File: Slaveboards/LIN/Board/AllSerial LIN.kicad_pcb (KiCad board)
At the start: 2 copper layers, 67.4 x 44.8 mm, 13 parts, among them IC6 MCP2003, J1 MA02-1W, X1 ALLSERIALSLAVE, X6 AKL18X-03W

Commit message: Improve libraries
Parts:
- moved X6 1.27 mm to (161.2, 91.2)
- moved D2 1.15 mm to (157.9, 100.1)
- moved C1 0.82 mm to (159.3, 95.2)
- moved J1 0.49 mm to (134.5, 91.7)
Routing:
- net Net-(D2-K): track 42.5 -> 43.9 mm
- net GND: track 10.8 -> 11.6 mm, vias 43 -> 42
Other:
- board text added: "AllSerial - LIN v1.3 27/25"
- board text removed: "AllSerial - LIN v1.2 25/23"
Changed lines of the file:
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@@
 	(footprint "Diode_SMD:D_SMB"
 		(layer "F.Cu")
-		(at 157.8991 98.9556 180)
+		(at 157.8991 100.1036 180)
 		(descr "Diode SMB (DO-214AA)")
 		(tags "Diode SMB (DO-214AA)")
@@
 	(footprint "Connector_PinHeader_2.54mm:PinHeader_1x02_P2.54mm_Horizontal"
 		(layer "F.Cu")
-		(at 134.5311 91.2086 90)
+		(at 134.5311 91.7036 90)
 		(descr "Through hole angled pin header, 1x02, 2.54mm pitch, 6mm pin length, single row")
 		(tags "Through hole angled pin header THT 1x02 2.54mm single row")
@@
 	(footprint "AllSerial:Metz_PT11303HBBN_182"
 		(layer "F.Cu")
-		(at 161.2011 89.9386 180)
+		(at 161.2011 91.2036 180)
 		(property "Reference" "X6"
 			(at -0.7989 -4.0614 180)
@@
 	(footprint "Capacitor_SMD:C_0805_2012Metric"
 		(layer "F.Cu")
-		(at 159.2961 94.3836 180)
+		(at 159.2961 95.2036 180)
 		(descr "Capacitor SMD 0805 (2012 Metric), square (rectangular) end terminal, IPC_7351 nominal, (Body size source: IPC-SM-782 page 76, https://www.pcb-3d.com/wordpress/wp-content/uploads/ipc-sm-782a_amendment_1_and_2.pdf, https://docs.google.com/spreadsheets/d/1BsfQQcO9C6DZCsRaXUlFlo91Tg2WpOkGARC1WS5S8t0/edit?usp=sharing), generated with kicad-footprint-generator")
 		(tags "capacitor")
@@
 			(stroke
 				(width 0.1)
-				(type solid)
+				(type dash)
+			)
+			(layer "Dwgs.User")
+		)
+		(fp_line
+			(start -35.75 -45.8)
+			(end 35.75 -45.8)
+			(stroke
+				(width 0.1)
+				(type dash)
 			)
 			(layer "Dwgs.User")
@@
 		)
 		(embedded_fonts no)
-		(model ":KICAD9_3DMODEL_DIR:Connector_PinHeader_2.54mm.3dshapes/PinHeader_2x10_P2.54mm_Horizontal.step"
+		(model "$(KICAD8_3DMODEL_DIR)/Connector_PinHeader_2.54mm.3dshapes/PinHeader_2x10_P2.54mm_Horizontal.step"
 			(offset
 				(xyz 11.43 7 0)
@@
 			)
 		)
-		(model "../Front/AllSerial LIN Front.step"
+		(model "${KICAD9_3RD_PARTY}/packages3d/Fischer AKG 71 24 100 bottom half.step"
+			(offset
+				(xyz 35.8 44.8 1.85)
+			)
+			(scale
+				(xyz 1 1 1)
+			)
+			(rotate
+				(xyz 90 0 -180)
+			)
+		)
+		(model "C:/Users/StefanSeegel/Dropbox/Projekte/AllSerial Repo/Slaveboards/LIN/Front/AllSerial LIN Front.step"
 			(offset
-				(xyz 0 44.8 -7.2)
+				(xyz 0 44.8 -7.25)
 			)
 			(scale
@@
 		)
 	)
-	(gr_text "AllSerial - LIN v1.2 25/23"
+	(gr_text "AllSerial - LIN v1.3 27/25"
 		(at 118.0211 118.5136 90)
 		(layer "F.SilkS")
@@
 	)
 	(segment
-		(start 158.3461 94.3836)
-		(end 158.3461 93.4336)
+		(start 158.3461 93.4336)
+		(end 157.7011 92.7886)
 		(width 0.4064)
 		(layer "F.Cu")
@@
 	)
 	(segment
-		(start 157.7011 92.7886)
+		(start 158.3461 95.2036)
 		(end 158.3461 93.4336)
 		(width 0.4064)
@@
 	)
 	(segment
-		(start 159.2961 105.5596)
-		(end 160.3121 105.5596)
+		(start 157.7011 92.7886)
+		(end 157.7011 89.9386)
 		(width 0.4064)
 		(layer "F.Cu")
@@
 	)
 	(segment
-		(start 153.5811 109.3036)
-		(end 153.5811 110.8936)
+		(start 159.2961 105.5596)
+		(end 160.3121 105.5596)
 		(width 0.4064)
 		(layer "F.Cu")
@@
 	)
 	(segment
-		(start 157.7011 89.9386)
-		(end 157.7011 92.7886)
+		(start 153.5811 109.3036)
+		(end 153.5811 110.8936)
 		(width 0.4064)
 		(layer "F.Cu")
@@
 	)
 	(via
-		(at 148.5011 114.7036)
-		(size 0.6048)
-		(drill 0.3)
-		(layers "F.Cu" "B.Cu")
-		(net 1)
-	)
-	(via
 		(at 173.9011 114.7036)
 		(size 0.6048)
@@
 	)
 	(segment
-		(start 137.0711 120.4186)
-		(end 137.0711 119.7836)
+		(start 147.2311 114.7036)
+		(end 142.1511 119.7836)
 		(width 0.4064)
 		(layer "F.Cu")
@@
 	)
 	(segment
-		(start 148.5011 115.9736)
-		(end 145.9611 115.9736)
+		(start 137.0711 120.4186)
+		(end 137.0711 119.7836)
 		(width 0.4064)
 		(layer "F.Cu")
@@
 	)
 	(segment
-		(start 145.9611 115.9736)
-		(end 142.1511 119.7836)
-		(width 0.4064)
-		(layer "F.Cu")
-		(net 2)
-	)
-	(segment
 		(start 156.7561 111.1476)
 		(end 156.7561 114.0686)
@@
 	)
 	(segment
-		(start 149.7711 114.7036)
-		(end 148.5011 115.9736)
+		(start 151.0411 114.7036)
+		(end 147.2311 114.7036)
 		(width 0.4064)
 		(layer "F.Cu")
@@
 	)
 	(segment
-		(start 151.0411 114.7036)
-		(end 149.7711 114.7036)
-		(width 0.4064)
-		(layer "F.Cu")
-		(net 2)
-	)
-	(segment
 		(start 140.8811 118.5136)
 		(end 142.1511 119.7836)
@@
 	)
 	(segment
-		(start 161.2011 89.9386)
+		(start 160.2461 96.1616)
+		(end 160.2461 97.3036)
+		(width 0.4)
+		(layer "F.Cu")
+		(net 18)
+	)
+	(segment
+		(start 160.2461 94.0686)
 		(end 161.2011 93.1136)
 		(width 0.4064)
@@
 	)
 	(segment
+		(start 160.2461 96.1616)
+		(end 160.2461 95.2036)
+		(width 0.4)
+		(layer "F.Cu")
+		(net 18)
+	)
+	(segment
 		(start 159.9311 101.4956)
 		(end 159.9311 99.0736)
@@
 	)
 	(segment
-		(start 151.9301 91.2086)
-		(end 137.0711 91.2086)
-		(width 0.4)
+		(start 161.2011 93.1136)
+		(end 161.2011 89.9386)
+		(width 0.4064)
 		(layer "F.Cu")
 		(net 18)
@@
 	)
 	(segment
-		(start 158.0261 105.8786)
-		(end 158.0261 103.4006)
-		(width 0.2)
+		(start 152.4251 91.7036)
+		(end 137.0711 91.7036)
+		(width 0.4)
 		(layer "F.Cu")
 		(net 18)
 	)
 	(segment
-		(start 160.2461 94.3836)
-		(end 160.2461 94.0686)
-		(width 0.4064)
+		(start 158.0261 105.8786)
+		(end 158.0261 103.4006)
+		(width 0.2)
 		(layer "F.Cu")
 		(net 18)
@@
 	)
 	(segment
-		(start 160.2461 94.0686)
-		(end 161.2011 93.1136)
-		(width 0.4064)
-		(layer "F.Cu")
-		(net 18)
-	)
-	(segment
-		(start 160.2461 96.1616)
-		(end 160.2461 94.3836)
+		(start 158.0251 97.3036)
+		(end 152.4251 91.7036)
 		(width 0.4)
 		(layer "F.Cu")
@@
 	)
 	(segment
-		(start 156.8831 96.1616)
-		(end 151.9301 91.2086)
+		(start 160.2461 97.3036)
+		(end 158.0251 97.3036)
 		(width 0.4)
 		(layer "F.Cu")
@@
 	)
 	(segment
-		(start 160.2461 96.1616)
-		(end 156.8831 96.1616)
-		(width 0.4)
+		(start 158.0261 103.4006)
+		(end 159.9311 101.4956)
+		(width 0.2)
 		(layer "F.Cu")
 		(net 18)
 	)
 	(segment
-		(start 158.0261 103.4006)
-		(end 159.9311 101.4956)
-		(width 0.2)
+		(start 160.2461 95.2036)
+		(end 160.2461 94.0686)
+		(width 0.4064)
 		(layer "F.Cu")
 		(net 18)
@@
 	(segment
 		(start 134.5311 89.3036)
-		(end 134.5311 91.2086)
+		(end 134.5311 91.7036)
 		(width 0.3048)
 		(layer "F.Cu")
@@
 	)
 	(segment
-		(start 142.4711 88.0336)
-		(end 135.8011 88.0336)
+		(start 135.8011 88.0336)
+		(end 134.5311 89.3036)
 		(width 0.3048)
 		(layer "F.Cu")
@@
 	)
 	(segment
-		(start 135.8011 88.0336)
-		(end 134.5311 89.3036)
+		(start 142.4711 88.0336)
+		(end 135.8011 88.0336)
 		(width 0.3048)
 		(layer "F.Cu")

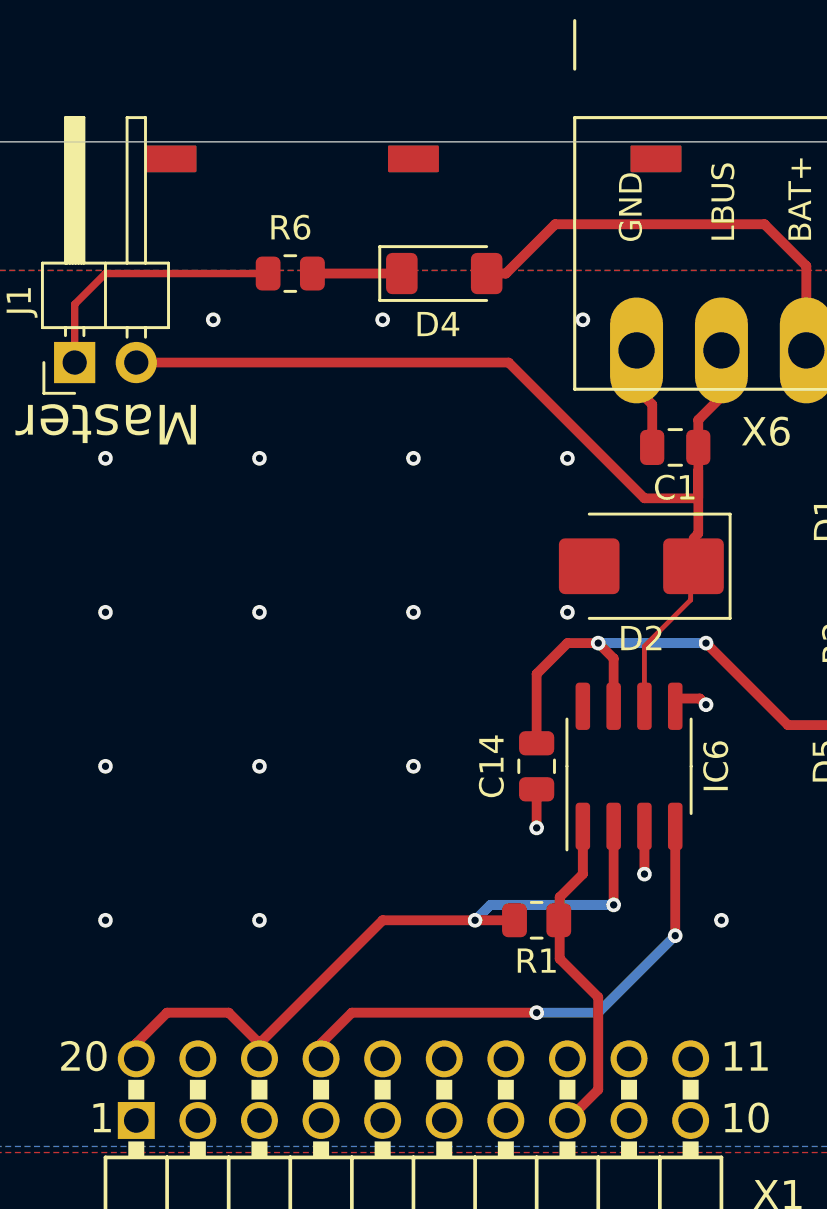
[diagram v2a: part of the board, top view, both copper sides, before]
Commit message: FTDI master: Change footprint of isolators
minor improvments
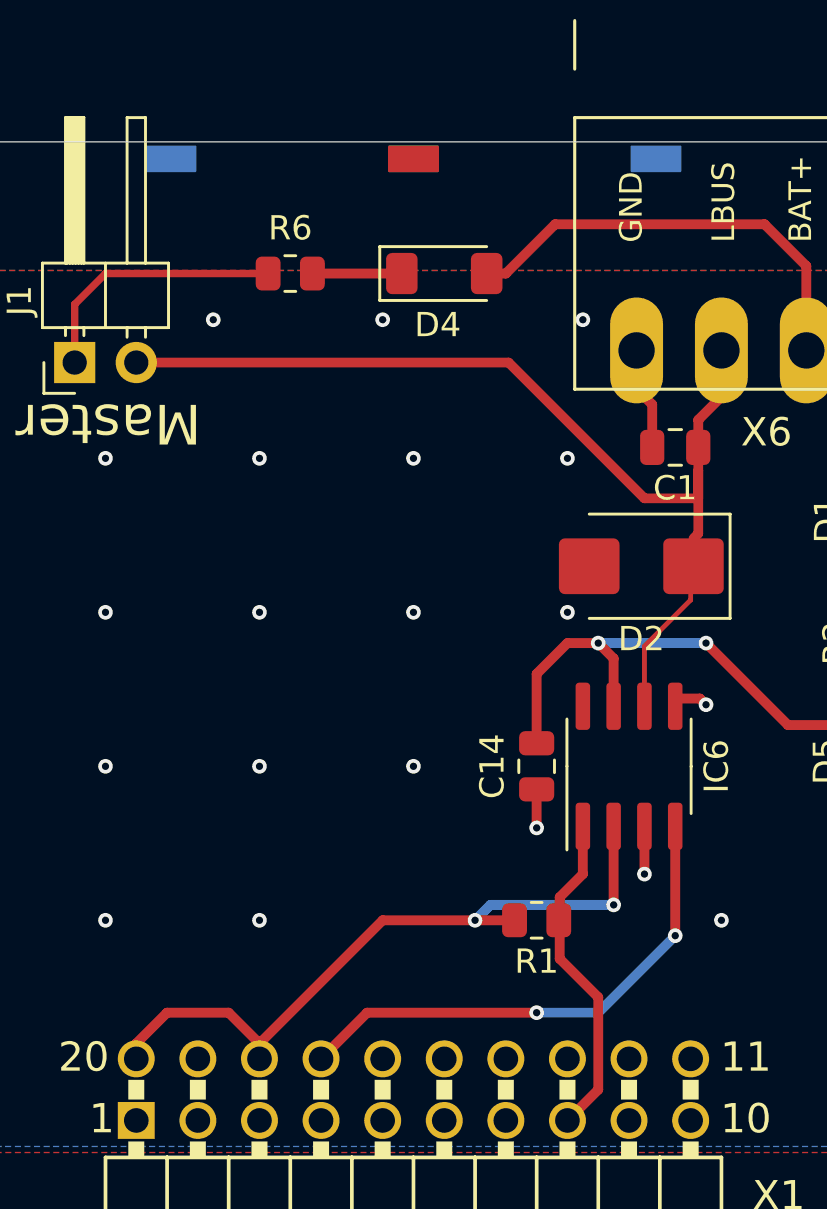
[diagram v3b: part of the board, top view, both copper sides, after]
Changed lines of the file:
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@@
-		)
-		(fp_rect
-			(start -11 -44.6)
-			(end -9 -43.6)
-			(stroke
-				(width 0.1)
-				(type solid)
-			)
-			(fill yes)
-			(layer "F.Cu")
 		)
 		(fp_rect
@@
 		)
 		(fp_rect
-			(start 9 -44.6)
-			(end 11 -43.6)
-			(stroke
-				(width 0.1)
-				(type solid)
-			)
-			(fill yes)
-			(layer "F.Cu")
-		)
-		(fp_rect
 			(start 19 -44.6)
 			(end 21 -43.6)
@@
 		)
 		(fp_rect
-			(start -11 -44.6)
-			(end -9 -43.6)
-			(stroke
-				(width 0.1)
-				(type solid)
-			)
-			(fill yes)
-			(layer "F.Mask")
-		)
-		(fp_rect
 			(start -1 -44.6)
 			(end 1 -43.6)
-			(stroke
-				(width 0.1)
-				(type solid)
-			)
-			(fill yes)
-			(layer "F.Mask")
-		)
-		(fp_rect
-			(start 9 -44.6)
-			(end 11 -43.6)
 			(stroke
 				(width 0.1)
@@
 	)
 	(segment
+		(start 146.5911 118.5136)
+		(end 153.5811 118.5136)
+		(width 0.4064)
+		(layer "F.Cu")
+		(net 4)
+	)
+	(segment
 		(start 159.2961 111.1476)
 		(end 159.2961 115.3386)
@@
 	)
 	(segment
-		(start 144.6911 120.4186)
-		(end 144.6911 119.7836)
+		(start 144.6911 120.4136)
+		(end 146.5911 118.5136)
 		(width 0.4064)
 		(layer "F.Cu")
@@
 	)
 	(segment
-		(start 144.6911 119.7836)
-		(end 145.9611 118.5136)
+		(start 144.6911 120.4186)
+		(end 144.6911 120.4136)
 		(width 0.4064)
 		(layer "F.Cu")
-		(net 4)
-	)
-	(segment
-		(start 145.9611 118.5136)
-		(end 153.5811 118.5136)
-		(width 0.4064)
-		(layer "F.Cu")
